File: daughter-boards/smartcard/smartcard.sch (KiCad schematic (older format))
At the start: 46 parts, among them P1 SAMTEC-QSE-020-01-F-D-A, P2 SAMTEC-QSE-020-01-F-D-A, U1 7334L2622F04LF

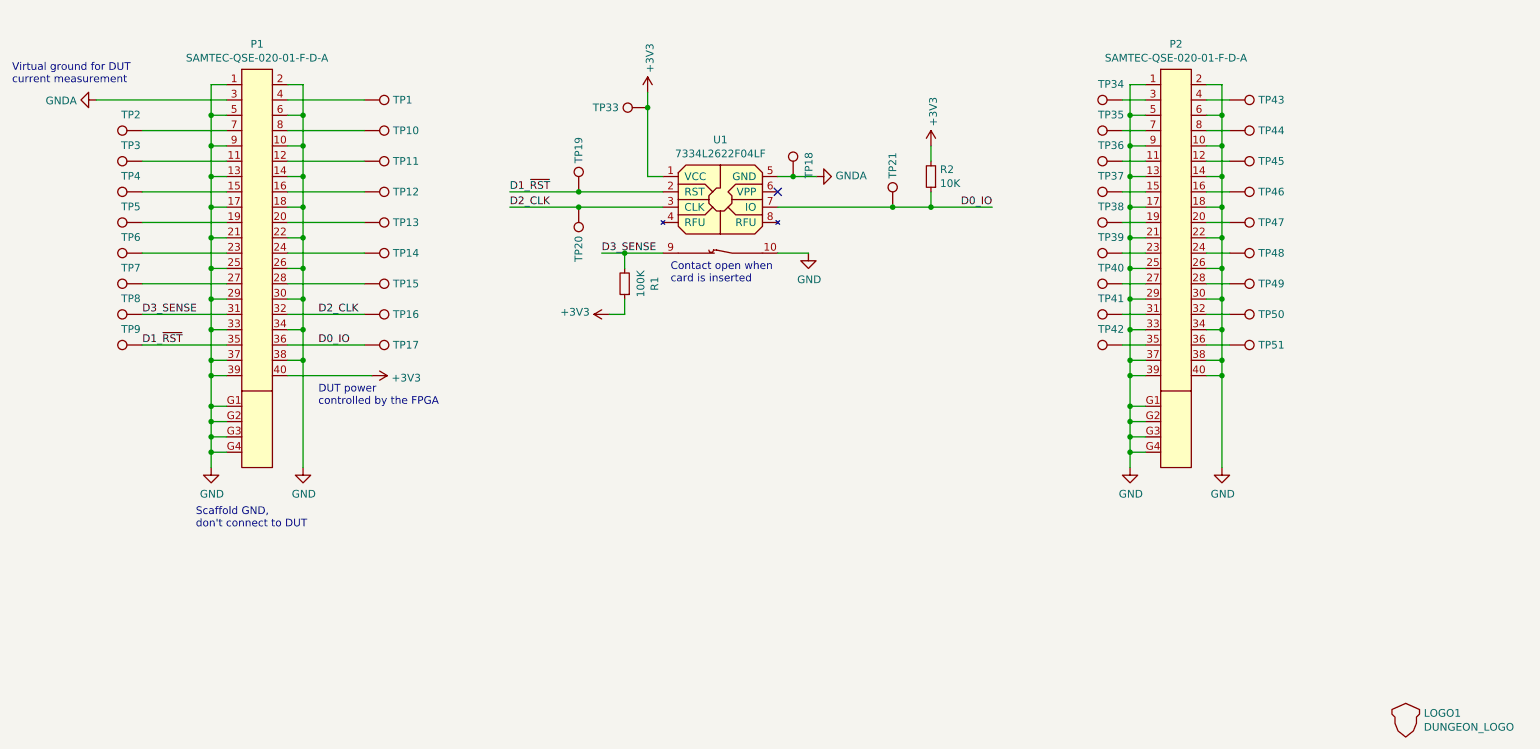
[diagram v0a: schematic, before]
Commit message: Updated daughterboards for the new Scaffold socket
Update breadboard, smartcard and STM32F205 daughterboards to fit the
new socket format of Scaffold v1.1 hardware.
Previous socket format is now deprecated.
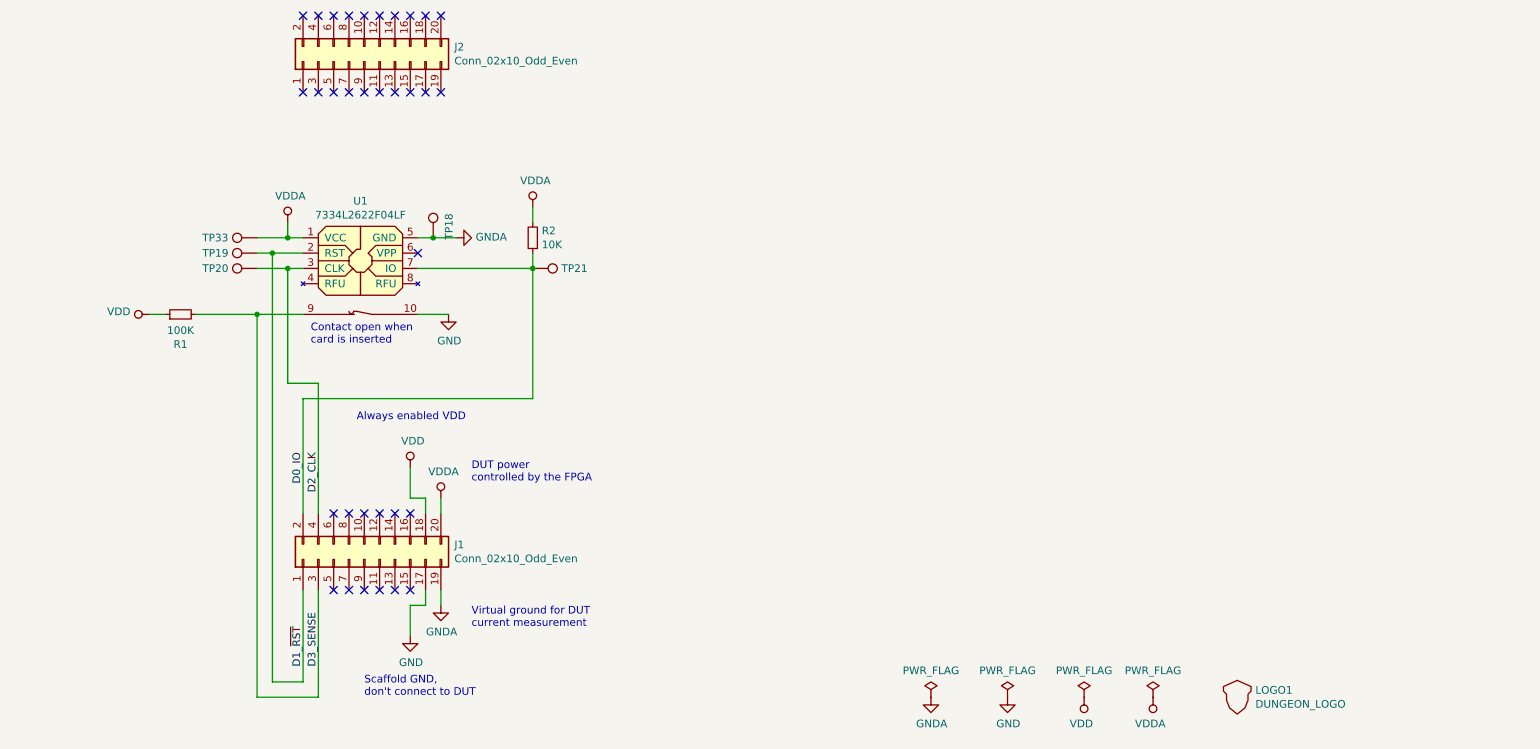
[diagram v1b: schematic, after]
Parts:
- removed P1, P2: SAMTEC-QSE-020-01-F-D-A, mykicadlibs:SAMTEC-QSE-020-01-F-D-A, symbol mylib:SAMTEC-QSE-020-01-F-D-A
- removed TP1, TP10, TP11, TP12, TP13, TP14, TP15, TP16, TP17, TP2, TP3, TP34, TP35, TP36, TP37, TP38, TP39, TP4, TP40, TP41, TP42, TP43, TP44, TP45, TP46, TP47, TP48, TP49, TP5, TP50, TP51, TP6, TP7, TP8, TP9: TestPoint, TestPoint:TestPoint_Pad_D1.5mm, symbol Connector:TestPoint
- added J1, J2: Conn_02x10_Odd_Even, Connector_PinSocket_2.54mm:PinSocket_2x10_P2.54mm_Vertical, symbol Connector_Generic:Conn_02x10_Odd_Even
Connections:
- net D0_IO: now also J1.2 (Pin_2)
- net D1_~RST~: now also J1.1 (Pin_1)
- net D2_CLK: now also J1.4 (Pin_4)
- net D3_SENSE: now also J1.3 (Pin_3)
- net GND: now also J1.17 (Pin_17)
- net GNDA: now also J1.19 (Pin_19)
- net +3V3 renamed VDDA
- net VDDA: now also J1.20 (Pin_20); no longer R1.1
- new net VDD: J1.18 (Pin_18), R1.1
- no-connect marks 1 -> 33
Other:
- note added: "Always enabled VDD"
- moved on the sheet: LOGO1, R1, R2, TP18, TP19, TP20, TP21, TP33, U1
